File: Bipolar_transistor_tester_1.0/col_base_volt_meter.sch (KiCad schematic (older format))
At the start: 9 parts, among them Q1 PVG612, U3 CPC1977, U4 OP07

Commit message: tester up
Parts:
- added C21, C22: 100n, Capacitor_SMD:C_0805_2012Metric, symbol Device:C
- added R? (x3): 1k 1%, Resistor_SMD:R_0805_2012Metric, symbol Device:R
- C23: renamed from C3; value 100p -> 100n
- RV2: value 20k -> PV32H203; footprint (none) -> Potentiometer_THT:Potentiometer_Bourns_3339H_Vertical
- U22: renamed from U3; footprint (none) -> OptoDevice:i4-PAC
- U25: renamed from U4; footprint (none) -> Package_DIP:DIP-8_W7.62mm
- renumbered R7 to R36, R8 to R37, R9 to R38, Q1 to U23, D4 to U24
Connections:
- net labels added: 8_cbvm1, 8_cbvm2, 8_cbvm3, 8_com_an, adc2
- net labels removed: out
- wire segments 30 -> 54
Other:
- moved on the sheet: C23, R36, R37, R38, RV2, U22, U23, U24, U25

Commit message: tester up
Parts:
- gave numbers to parts that had none: 3
- renumbered R36 to R46, R37 to R47, R38 to R49
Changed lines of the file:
@@
 Sheet 6 11
 Title ""
-Date ""
+Date "2022-04-25"
 Rev ""
 Comp ""
@@
 $EndComp
 $Comp
-L Device:R R36
+L Device:R R46
 U 1 1 6262A676
 P 6400 3150
-F 0 "R36" V 6193 3150 50  0000 C CNN
+F 0 "R46" V 6193 3150 50  0000 C CNN
 F 1 "1M 1%" V 6284 3150 50  0000 C CNN
 F 2 "Resistor_SMD:R_0805_2012Metric" V 6330 3150 50  0001 C CNN
@@
 $EndComp
 $Comp
-L Device:R R37
+L Device:R R47
 U 1 1 6262A8A7
 P 6400 3850
-F 0 "R37" H 6470 3896 50  0000 L CNN
+F 0 "R47" H 6470 3896 50  0000 L CNN
 F 1 "200k 1%" H 6470 3805 50  0000 L CNN
 F 2 "Resistor_SMD:R_0805_2012Metric" V 6330 3850 50  0001 C CNN
@@
 base_in
 $Comp
-L power:+15V #PWR079
+L power:+15V #PWR092
 U 1 1 626391AB
 P 7150 2800
-F 0 "#PWR079" H 7150 2650 50  0001 C CNN
+F 0 "#PWR092" H 7150 2650 50  0001 C CNN
 F 1 "+15V" H 7165 2973 50  0000 C CNN
 F 2 "" H 7150 2800 50  0001 C CNN
@@
 	7150 2800 7150 2950
 $Comp
-L power:-15V #PWR080
+L power:-15V #PWR093
 U 1 1 62639872
 P 7150 3700
-F 0 "#PWR080" H 7150 3800 50  0001 C CNN
+F 0 "#PWR093" H 7150 3800 50  0001 C CNN
 F 1 "-15V" H 7165 3873 50  0000 C CNN
 F 2 "" H 7150 3700 50  0001 C CNN
@@
 	7150 3700 7150 3550
 $Comp
-L power:GND #PWR078
+L power:GND #PWR091
 U 1 1 6263A605
 P 6400 4100
-F 0 "#PWR078" H 6400 3850 50  0001 C CNN
+F 0 "#PWR091" H 6400 3850 50  0001 C CNN
 F 1 "GND" H 6405 3927 50  0000 C CNN
 F 2 "" H 6400 4100 50  0001 C CNN
@@
 NoConn ~ 6450 2750
 $Comp
-L Device:R R38
+L Device:R R49
 U 1 1 6263B5E8
 P 8000 3250
-F 0 "R38" V 8207 3250 50  0000 C CNN
+F 0 "R49" V 8207 3250 50  0000 C CNN
 F 1 "100" V 8116 3250 50  0000 C CNN
 F 2 "Resistor_SMD:R_0805_2012Metric" V 7930 3250 50  0001 C CNN
@@
 Connection ~ 8350 3250
 $Comp
-L power:GND #PWR082
+L power:GND #PWR095
 U 1 1 6263D5AF
 P 8350 3700
-F 0 "#PWR082" H 8350 3450 50  0001 C CNN
+F 0 "#PWR095" H 8350 3450 50  0001 C CNN
 F 1 "GND" H 8355 3527 50  0000 C CNN
 F 2 "" H 8350 3700 50  0001 C CNN
@@
 	7750 4050 7750 4000
 $Comp
-L power:+15V #PWR081
+L power:+15V #PWR094
 U 1 1 626436F2
 P 7900 3650
-F 0 "#PWR081" H 7900 3500 50  0001 C CNN
+F 0 "#PWR094" H 7900 3500 50  0001 C CNN
 F 1 "+15V" H 7915 3823 50  0000 C CNN
 F 2 "" H 7900 3650 50  0001 C CNN
@@
 AR Path="/62558810/62AD0B47" Ref="#PWR?"  Part="1"
 AR Path="/62558C62/62AD0B47" Ref="#PWR?"  Part="1"
-AR Path="/625CBB4F/62AD0B47" Ref="#PWR075"  Part="1"
-F 0 "#PWR075" H 3500 5300 50  0001 C CNN
+AR Path="/625CBB4F/62AD0B47" Ref="#PWR088"  Part="1"
+F 0 "#PWR088" H 3500 5300 50  0001 C CNN
 F 1 "-15V" H 3515 5373 50  0000 C CNN
 F 2 "" H 3500 5200 50  0001 C CNN
@@
 AR Path="/62558810/62AD0B4D" Ref="#PWR?"  Part="1"
 AR Path="/62558C62/62AD0B4D" Ref="#PWR?"  Part="1"
-AR Path="/625CBB4F/62AD0B4D" Ref="#PWR077"  Part="1"
-F 0 "#PWR077" H 3950 5050 50  0001 C CNN
+AR Path="/625CBB4F/62AD0B4D" Ref="#PWR090"  Part="1"
+F 0 "#PWR090" H 3950 5050 50  0001 C CNN
 F 1 "+15V" H 3965 5373 50  0000 C CNN
 F 2 "" H 3950 5200 50  0001 C CNN
@@
 AR Path="/62558810/62AD0B56" Ref="#PWR?"  Part="1"
 AR Path="/62558C62/62AD0B56" Ref="#PWR?"  Part="1"
-AR Path="/625CBB4F/62AD0B56" Ref="#PWR076"  Part="1"
-F 0 "#PWR076" H 3750 5500 50  0001 C CNN
+AR Path="/625CBB4F/62AD0B56" Ref="#PWR089"  Part="1"
+F 0 "#PWR089" H 3750 5500 50  0001 C CNN
 F 1 "GND" H 3755 5577 50  0000 C CNN
 F 2 "" H 3750 5750 50  0001 C CNN
@@
 8_com_an
 $Comp
-L Device:R R?
+L Device:R R44
 U 1 1 62832F02
 P 4700 4000
-F 0 "R?" H 4550 3950 50  0000 C CNN
+F 0 "R44" H 4550 3950 50  0000 C CNN
 F 1 "1k 1%" H 4500 4050 50  0000 C CNN
 F 2 "Resistor_SMD:R_0805_2012Metric" V 4630 4000 50  0001 C CNN
@@
 8_com_an
 $Comp
-L Device:R R?
+L Device:R R48
 U 1 1 62836070
 P 6550 1900
-F 0 "R?" H 6700 1950 50  0000 C CNN
+F 0 "R48" H 6700 1950 50  0000 C CNN
 F 1 "1k 1%" H 6750 1850 50  0000 C CNN
 F 2 "Resistor_SMD:R_0805_2012Metric" V 6480 1900 50  0001 C CNN
@@
 8_com_an
 $Comp
-L Device:R R?
+L Device:R R45
 U 1 1 628379E9
 P 5600 5400
-F 0 "R?" H 5450 5350 50  0000 C CNN
+F 0 "R45" H 5450 5350 50  0000 C CNN
 F 1 "1k 1%" H 5400 5450 50  0000 C CNN
 F 2 "Resistor_SMD:R_0805_2012Metric" V 5530 5400 50  0001 C CNN

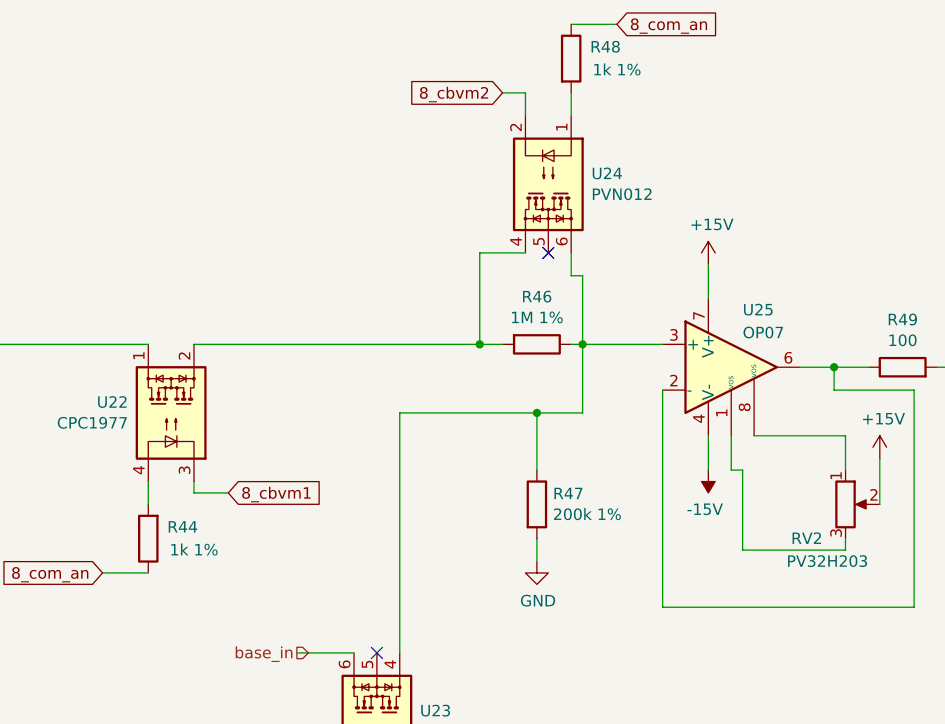
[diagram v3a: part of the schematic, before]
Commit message: edit resistors cpc1977
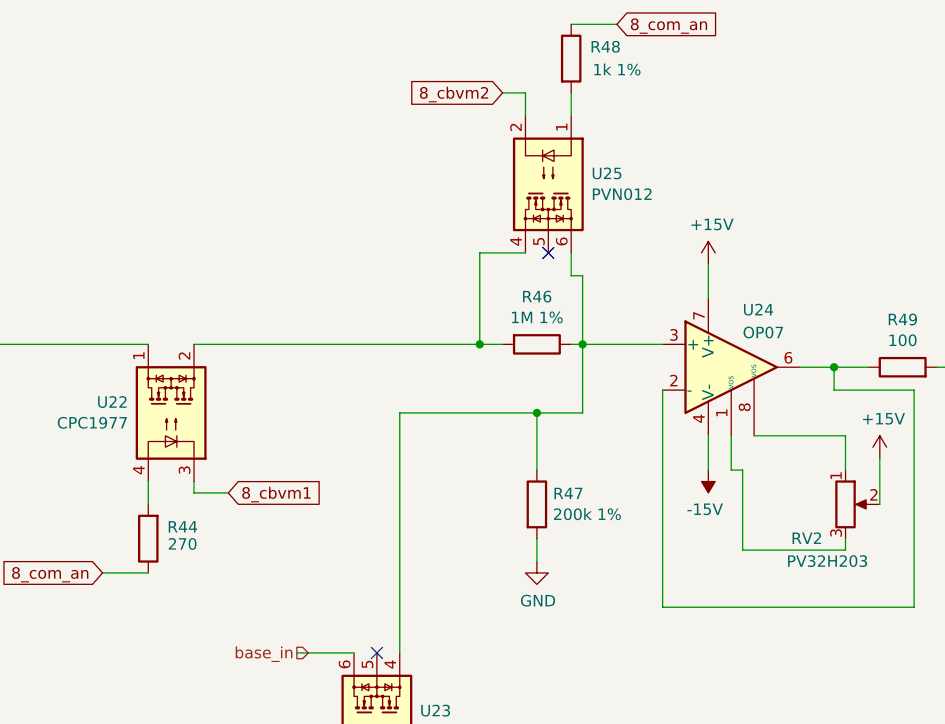
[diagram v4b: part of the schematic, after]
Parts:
- R44: value 1k 1% -> 270
- renumbered U25 to U24, U24 to U25
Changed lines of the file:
@@
 $EndDescr
 $Comp
-L Amplifier_Operational:OP07 U25
+L Amplifier_Operational:OP07 U24
 U 1 1 6262629F
 P 7250 3250
-F 0 "U25" H 7300 3500 50  0000 L CNN
+F 0 "U24" H 7300 3500 50  0000 L CNN
 F 1 "OP07" H 7300 3400 50  0000 L CNN
 F 2 "Package_DIP:DIP-8_W7.62mm" H 7300 3300 50  0001 C CNN
@@
 $EndComp
 $Comp
-L Relay_SolidState:PVN012 U24
+L Relay_SolidState:PVN012 U25
 U 1 1 62628190
 P 6450 2450
-F 0 "U24" V 6404 2638 50  0000 L CNN
+F 0 "U25" V 6404 2638 50  0000 L CNN
 F 1 "PVN012" V 6495 2638 50  0000 L CNN
 F 2 "Package_DIP:DIP-6_W7.62mm" H 6470 2650 50  0001 C CNN
@@
 P 4700 4000
 F 0 "R44" H 4550 3950 50  0000 C CNN
-F 1 "1k 1%" H 4500 4050 50  0000 C CNN
+F 1 "270" H 4550 4025 50  0000 C CNN
 F 2 "Resistor_SMD:R_0805_2012Metric" V 4630 4000 50  0001 C CNN
 F 3 "~" H 4700 4000 50  0001 C CNN
